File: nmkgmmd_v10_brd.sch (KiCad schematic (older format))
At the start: 3 parts

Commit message: 石を303CC(48pin)に変更，少しだけピンを引き出した
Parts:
- removed C? (x2): C, symbol C
- removed U?: STM32F303RETx, LQFP64, symbol STM32F303RETx
- added L?: L, symbol L
- added U?: STM32F313CCTx, LQFP48, symbol STM32F313CCTx
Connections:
- net labels added: ADC1_IN1, ADC1_IN2, ADC2_IN1, ADC3_IN1, ADC4_IN3, GD_FAULT1, GD_FAULT2, GD_RESET1, GD_RESET2, LED0, LED1, LED2, SWCLK, SWDIO, TIM15_CH2, TIM1_CH1, TIM1_CH1N, TIM1_CH2, TIM1_CH2N, TIM2_CH1, TIM2_CH2, TIM3_CH1, TIM3_CH2, TIM4_CH2, TIM8_CH1, TIM8_CH1N, TIM8_CH2, TIM8_CH2N, USART3RX, USART3TX
- wire segments 29 -> 23
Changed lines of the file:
@@
 LIBS:valves
 LIBS:stm32
+LIBS:nmkgmmd_v10_brd-cache
 EELAYER 25 0
 EELAYER END
@@
 Comment4 ""
 $EndDescr
-$Comp
-L STM32F303RETx U?
-U 1 1 58989F63
-P 8250 5300
-F 0 "U?" H 3150 7225 50  0000 L BNN
-F 1 "STM32F303RETx" H 13350 7225 50  0000 R BNN
-F 2 "LQFP64" H 13350 7175 50  0000 R TNN
-F 3 "" H 8250 5300 50  0000 C CNN
-	1    8250 5300
-	1    0    0    -1
-$EndComp
 $Comp
 L GND #PWR?
@@
 	1    0    0    -1
 $EndComp
-$Comp
-L C C?
-U 1 1 5898A2BF
-P 1700 4800
-F 0 "C?" H 1725 4900 50  0000 L CNN
-F 1 "C" H 1725 4700 50  0000 L CNN
-F 2 "" H 1738 4650 50  0001 C CNN
-F 3 "" H 1700 4800 50  0001 C CNN
-	1    1700 4800
-	0    1    1    0
-$EndComp
-$Comp
-L C C?
-U 1 1 5898A3A8
-P 1700 5100
-F 0 "C?" H 1725 5200 50  0000 L CNN
-F 1 "C" H 1725 5000 50  0000 L CNN
-F 2 "" H 1738 4950 50  0001 C CNN
-F 3 "" H 1700 5100 50  0001 C CNN
-	1    1700 5100
-	0    1    1    0
-$EndComp
-$Comp
-L GND #PWR?
-U 1 1 5898A3C8
-P 1450 4950
-F 0 "#PWR?" H 1450 4700 50  0001 C CNN
-F 1 "GND" H 1450 4800 50  0000 C CNN
-F 2 "" H 1450 4950 50  0001 C CNN
-F 3 "" H 1450 4950 50  0001 C CNN
-	1    1450 4950
-	0    1    1    0
-$EndComp
 Wire Wire Line
 	8050 7300 8050 7350
 Wire Wire Line
-	8050 7350 8150 7350
+	8050 7350 8350 7350
 Wire Wire Line
-	8150 7350 8200 7350
+	8350 7350 8350 7100
 Wire Wire Line
-	8200 7350 8250 7350
-Wire Wire Line
-	8250 7350 8350 7350
-Wire Wire Line
-	8350 7350 8350 7300
-Wire Wire Line
-	8150 7300 8150 7350
+	8150 7100 8150 7350
 Connection ~ 8150 7350
 Wire Wire Line
-	8250 7300 8250 7350
+	8250 7100 8250 7350
 Connection ~ 8250 7350
 Wire Wire Line
@@
 Connection ~ 8200 7350
 Wire Wire Line
-	8050 3300 8050 3250
-Wire Wire Line
-	8050 3250 8150 3250
-Wire Wire Line
-	8150 3250 8200 3250
-Wire Wire Line
-	8200 3250 8250 3250
-Wire Wire Line
-	8250 3250 8350 3250
+	8100 3250 8350 3250
 Wire Wire Line
 	8350 3250 8350 3300
@@
 Connection ~ 8200 3250
 Wire Wire Line
-	1550 4800 1500 4800
-Wire Wire Line
-	1500 4800 1500 4950
-Wire Wire Line
-	1500 4950 1500 5100
-Wire Wire Line
-	1500 5100 1550 5100
-Wire Wire Line
-	1450 4950 1500 4950
-Connection ~ 1500 4950
-Wire Wire Line
 	3050 5000 2350 5000
 Wire Wire Line
@@
 Wire Wire Line
 	2350 4800 2000 4800
+$Comp
+L STM32F313CCTx U?
+U 1 1 58ADBEE3
+P 8250 5200
+F 0 "U?" H 1750 7025 50  0000 L BNN
+F 1 "STM32F313CCTx" H 14750 7025 50  0000 R BNN
+F 2 "LQFP48" H 14750 6975 50  0001 R TNN
+F 3 "" H 8250 5200 50  0001 C CNN
+	1    8250 5200
+	1    0    0    -1
+$EndComp
+$Comp
+L L L?
+U 1 1 58ADC12E
+P 7850 3050
+F 0 "L?" V 7800 3050 50  0000 C CNN
+F 1 "L" V 7925 3050 50  0000 C CNN
+F 2 "" H 7850 3050 50  0001 C CNN
+F 3 "" H 7850 3050 50  0001 C CNN
+	1    7850 3050
+	0    -1   -1   0
+$EndComp
+Wire Wire Line
+	8100 3250 8100 3050
+Wire Wire Line
+	8100 3050 8000 3050
+Wire Wire Line
+	7700 3050 7650 3050
+Wire Wire Line
+	7650 3050 7650 3250
+Wire Wire Line
+	7650 3250 8050 3250
+Wire Wire Line
+	8050 3250 8050 3300
+Text HLabel 14850 5100 2    60   Input ~ 0
+ADC1_IN1
+Text HLabel 14850 5200 2    60   Input ~ 0
+ADC1_IN2
+Text HLabel 14850 5500 2    60   Input ~ 0
+ADC2_IN1
+Text HLabel 14850 5800 2    60   Output ~ 0
+TIM8_CH1N
+Text HLabel 14850 5900 2    60   Output ~ 0
+TIM1_CH1
+Text HLabel 14850 6000 2    60   Output ~ 0
+TIM1_CH2
+Text HLabel 14850 6100 2    60   Output ~ 0
+GD_RESET1
+Text HLabel 14850 6200 2    60   Output ~ 0
+GD_RESET2
+Text HLabel 14850 6300 2    60   Output ~ 0
+TIM1_CH2N
+Text GLabel 14850 6400 2    60   Input ~ 0
+SWDIO
+Text GLabel 14850 6500 2    60   Input ~ 0
+SWCLK
+Text HLabel 14850 6600 2    60   Output ~ 0
+TIM2_CH1
+Text HLabel 1650 6600 0    60   Input ~ 0
+TIM15_CH2
+Text HLabel 1650 6500 0    60   Input ~ 0
+GD_FAULT1
+Text HLabel 1650 6400 0    60   Input ~ 0
+GD_FAULT2
+Text HLabel 1650 6300 0    60   Input ~ 0
+ADC4_IN3
+Text HLabel 1650 6200 0    60   Input ~ 0
+USART3RX
+Text HLabel 1650 6100 0    60   Output ~ 0
+USART3TX
+Text HLabel 1650 6000 0    60   Output ~ 0
+LED0
+Text HLabel 1650 5900 0    60   Output ~ 0
+TIM8_CH2
+Text HLabel 1650 5800 0    60   Output ~ 0
+TIM4_CH2
+Text HLabel 1650 5700 0    60   Output ~ 0
+TIM8_CH1
+Text HLabel 1650 5600 0    60   Input ~ 0
+TIM3_CH2
+Text HLabel 1650 5500 0    60   Input ~ 0
+TIM3_CH1
+Text HLabel 1650 5400 0    60   Input ~ 0
+TIM2_CH2
+Text HLabel 1650 5300 0    60   Input ~ 0
+ADC3_IN1
+Text HLabel 1650 5200 0    60   Output ~ 0
+TIM8_CH2N
+Text HLabel 1650 4800 0    60   Output ~ 0
+TIM1_CH1N
+Text HLabel 1650 4900 0    60   Output ~ 0
+LED1
+Text HLabel 1650 5000 0    60   Output ~ 0
+LED2
 $EndSCHEMATC

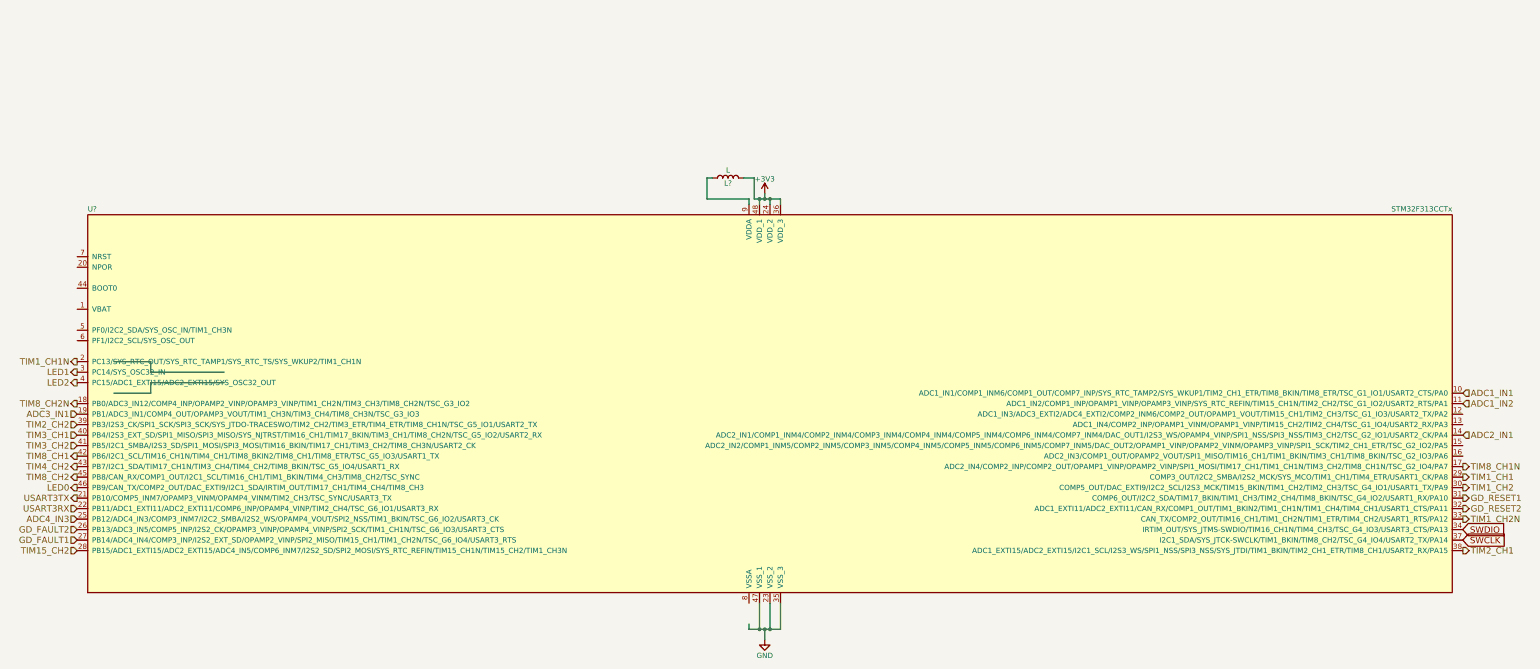
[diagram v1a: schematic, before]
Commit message: 制御回路完成，アノテーション
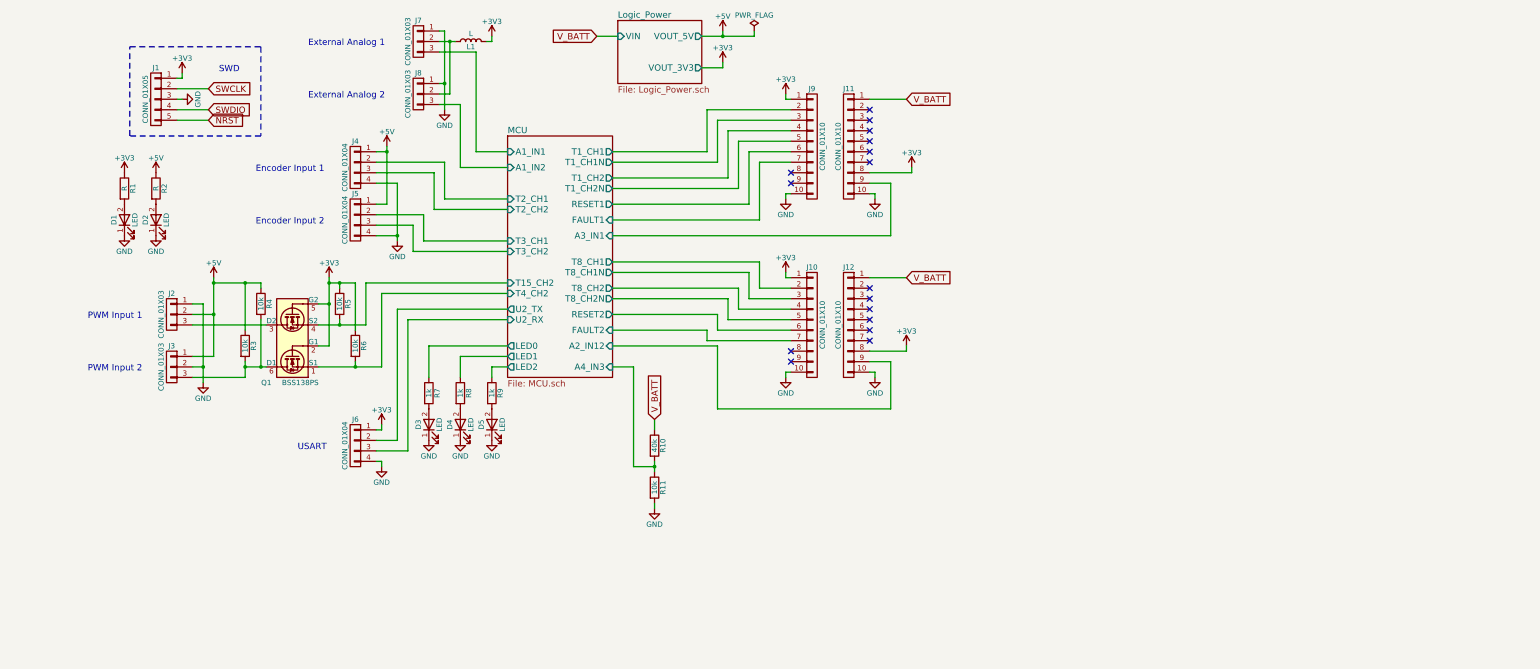
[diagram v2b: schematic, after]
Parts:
- removed L?: L, symbol L
- removed U?: STM32F313CCTx, LQFP48, symbol STM32F313CCTx
- added D1, D2, D3, D4, D5: LED, LEDs:LED_0603, symbol LED
- added J1: CONN_01X05, Connectors_JST:JST_ZH_S05B-ZR_05x1.50mm_Angled, symbol CONN_01X05
- added J10, J11, J12, J9: CONN_01X10, Pin_Headers:Pin_Header_Straight_1x10_Pitch2.00mm, symbol CONN_01X10
- added J2, J3, J7, J8: CONN_01X03, Connectors_JST:JST_ZH_S03B-ZR_03x1.50mm_Angled, symbol CONN_01X03
- added J4, J5, J6: CONN_01X04, Connectors_JST:JST_ZH_S04B-ZR_04x1.50mm_Angled, symbol CONN_01X04
- added L1: L, Inductors_NEOSID:Neosid_Inductor_SM0603CG, symbol L
- added Q1: BSS138PS, TO_SOT_Packages_SMD:SOT-363_SC-70-6, symbol BSS138PS
- added R1, R2: R, Resistors_SMD:R_0603, symbol R
- added R10: 40k, Resistors_SMD:R_0603, symbol R
- added R11, R3, R4, R5, R6: 10k, Resistors_SMD:R_0603, symbol R
- added R7, R8, R9: 1k, Resistors_SMD:R_0603, symbol R
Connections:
- net labels added: +5V, NRST, V_BATT
- net labels removed: ADC1_IN1, ADC1_IN2, ADC2_IN1, ADC3_IN1, ADC4_IN3, GD_FAULT1, GD_FAULT2, GD_RESET1, GD_RESET2, LED0, LED1, LED2, TIM15_CH2, TIM1_CH1, TIM1_CH1N, TIM1_CH2, TIM1_CH2N, TIM2_CH1, TIM2_CH2, TIM3_CH1, TIM3_CH2, TIM4_CH2, TIM8_CH1, TIM8_CH1N, TIM8_CH2, TIM8_CH2N, USART3RX, USART3TX
- wire segments 23 -> 156
- no-connect marks 0 -> 16
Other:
- note added: "Encoder Input 1"
- note added: "Encoder Input 2"
- note added: "External Analog 1"
- note added: "External Analog 2"
- note added: "PWM Input 1"
- note added: "PWM Input 2"
- note added: "SWD"
- note added: "USART"

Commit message: 回路図作ってみた
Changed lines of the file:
@@
 $Descr A4 11693 8268
 encoding utf-8
-Sheet 1 3
+Sheet 1 5
 Title ""
 Date ""
@@
 Wire Wire Line
 	7650 4500 6750 4500
+$Sheet
+S 9500 5550 1200 800
+U 58CBAEB3
+F0 "Driver1" 60
+F1 "Driver.sch" 60
+$EndSheet
+$Sheet
+S 7950 5550 1400 800
+U 58CBB47A
+F0 "Driver2" 60
+F1 "Driver.sch" 60
+$EndSheet
 $EndSCHEMATC

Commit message: アノテーション前のセーブ
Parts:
- removed J11, J12: CONN_01X10, Pin_Headers:Pin_Header_Straight_1x10_Pitch2.00mm, symbol CONN_01X10
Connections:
- net +3V3: now also J10.5 (P5), J9.5 (P5); no longer J10.1 (P1), J9.1 (P1)
- net GND: now also J10.3 (P3), J9.3 (P3); no longer J10.10 (P10), J9.10 (P10)
- net MCU/A2_IN12: now also J10.1 (P1)
- net MCU/A3_IN1: now also J9.1 (P1)
- net MCU/FAULT1: now also J9.6 (P6); no longer J9.7 (P7)
- net MCU/FAULT2: now also J10.6 (P6); no longer J10.7 (P7)
- net MCU/RESET1: now also J9.4 (P4); no longer J9.6 (P6)
- net MCU/RESET2: now also J10.4 (P4); no longer J10.6 (P6)
- net MCU/T1_CH1: now also J9.7 (P7); no longer J9.2 (P2)
- net MCU/T1_CH1N: now also J9.8 (P8); no longer J9.3 (P3)
- net MCU/T1_CH2: now also J9.9 (P9); no longer J9.4 (P4)
- net MCU/T1_CH2N: now also J9.10 (P10); no longer J9.5 (P5)
- net MCU/T8_CH1: now also J10.7 (P7); no longer J10.2 (P2)
- net MCU/T8_CH1N: now also J10.8 (P8); no longer J10.3 (P3)
- net MCU/T8_CH2: now also J10.9 (P9); no longer J10.4 (P4)
- net MCU/T8_CH2N: now also J10.10 (P10); no longer J10.5 (P5)
- net V_BATT: now also J10.2 (P2), J9.2 (P2)
- no-connect marks 16 -> 0
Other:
- moved on the sheet: J9

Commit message: セーブ
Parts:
- J10, J9: footprint Pin_Headers:Pin_Header_Straight_1x10_Pitch2.00mm -> Pin_Headers:Pin_Header_Straight_1x10_Pitch2.00mm_SMD_Pin1Right
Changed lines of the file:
@@
 F 0 "J9" H 8700 3250 50  0000 C CNN
 F 1 "CONN_01X10" V 8800 2700 50  0000 C CNN
-F 2 "Pin_Headers:Pin_Header_Straight_1x10_Pitch2.00mm" H 8700 2700 50  0001 C CNN
+F 2 "Pin_Headers:Pin_Header_Straight_1x10_Pitch2.00mm_SMD_Pin1Right" H 8700 2700 50  0001 C CNN
 F 3 "" H 8700 2700 50  0001 C CNN
 	1    8700 2700
@@
 F 0 "J10" H 8650 5000 50  0000 C CNN
 F 1 "CONN_01X10" V 8750 4450 50  0000 C CNN
-F 2 "Pin_Headers:Pin_Header_Straight_1x10_Pitch2.00mm" H 8650 4450 50  0001 C CNN
+F 2 "Pin_Headers:Pin_Header_Straight_1x10_Pitch2.00mm_SMD_Pin1Right" H 8650 4450 50  0001 C CNN
 F 3 "" H 8650 4450 50  0001 C CNN
 	1    8650 4450
@@
 V_BATT
 $Comp
-L GND #PWR026
+L GND #PWR023
 U 1 1 58C4425D
 P 8450 4200
-F 0 "#PWR026" H 8450 3950 50  0001 C CNN
+F 0 "#PWR023" H 8450 3950 50  0001 C CNN
 F 1 "GND" H 8450 4050 50  0000 C CNN
 F 2 "" H 8450 4200 50  0001 C CNN
@@
 $EndComp
 $Comp
-L GND #PWR029
+L GND #PWR024
 U 1 1 58C68B7D
 P 7150 6200
-F 0 "#PWR029" H 7150 5950 50  0001 C CNN
+F 0 "#PWR024" H 7150 5950 50  0001 C CNN
 F 1 "GND" H 7150 6050 50  0000 C CNN
 F 2 "" H 7150 6200 50  0001 C CNN
@@
 	7800 2000 7600 2000
 $Comp
-L PWR_FLAG #FLG030
+L PWR_FLAG #FLG025
 U 1 1 58CAB0FE
 P 8100 1650
-F 0 "#FLG030" H 8100 1725 50  0001 C CNN
+F 0 "#FLG025" H 8100 1725 50  0001 C CNN
 F 1 "PWR_FLAG" H 8100 1800 50  0000 C CNN
 F 2 "" H 8100 1650 50  0001 C CNN
@@
 $EndSheet
 $Comp
-L +3V3 #PWR025
+L +3V3 #PWR026
 U 1 1 58C42440
 P 8450 4400
-F 0 "#PWR025" H 8450 4250 50  0001 C CNN
+F 0 "#PWR026" H 8450 4250 50  0001 C CNN
 F 1 "+3V3" H 8450 4540 50  0000 C CNN
 F 2 "" H 8450 4400 50  0001 C CNN

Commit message: 進捗，セーブ
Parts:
- J1: footprint Connectors_JST:JST_ZH_S05B-ZR_05x1.50mm_Angled -> Connectors_JST:JST_SH_BM05B-SRSS-TB_05x1.00mm_Straight
- J6: footprint Connectors_JST:JST_ZH_S04B-ZR_04x1.50mm_Angled -> Connectors_JST:JST_ZH_B04B-ZR_04x1.50mm_Straight
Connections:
- net at J2.3 (P3), Q1.3 (D2): now also R4.2
- net at J3.3 (P3), Q1.6 (D1), R3.2: no longer R4.2
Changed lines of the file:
@@
 F 0 "J6" H 4300 5850 50  0000 C CNN
 F 1 "CONN_01X04" V 4400 5600 50  0000 C CNN
-F 2 "Connectors_JST:JST_ZH_S04B-ZR_04x1.50mm_Angled" H 4300 5600 50  0001 C CNN
+F 2 "Connectors_JST:JST_ZH_B04B-ZR_04x1.50mm_Straight" H 4300 5600 50  0001 C CNN
 F 3 "" H 4300 5600 50  0001 C CNN
 	1    4300 5600
@@
 F 0 "J1" H 2400 2600 50  0000 C CNN
 F 1 "CONN_01X05" V 2500 2300 50  0000 C CNN
-F 2 "Connectors_JST:JST_ZH_S05B-ZR_05x1.50mm_Angled" H 2400 2300 50  0001 C CNN
+F 2 "Connectors_JST:JST_SH_BM05B-SRSS-TB_05x1.00mm_Straight" H 2400 2300 50  0001 C CNN
 F 3 "" H 2400 2300 50  0001 C CNN
 	1    2400 2300
@@
 Connection ~ 3250 4850
 Wire Wire Line
-	3400 4400 3400 4850
-Connection ~ 3400 4850
-Wire Wire Line
 	3250 4050 3250 4500
 Wire Wire Line
@@
 Wire Wire Line
 	7550 3850 6750 3850
+Wire Wire Line
+	3400 4400 3400 4450
+Connection ~ 3400 4450
 $EndSCHEMATC

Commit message: 進捗
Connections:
- net +5V: now also J3.2 (P2); no longer J3.1 (P1)
- net GND: now also J3.1 (P1); no longer J3.2 (P2)
- net MCU/T3_CH1: now also J5.3 (P3); no longer J5.2 (P2)
- net MCU/T3_CH2: now also J5.2 (P2); no longer J5.3 (P3)
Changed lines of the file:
@@
 	4600 2750 4600 3300
-Wire Wire Line
-	4500 3400 4950 3400
-Wire Wire Line
-	4500 3500 4850 3500
 Wire Wire Line
 	4600 3300 4500 3300
@@
 	5750 4150 4550 4150
 Wire Wire Line
-	4550 4150 4550 4850
+	4550 4850 4550 4150
 Wire Wire Line
 	4400 4050 5750 4050
@@
 	2850 4250 2850 5000
 Wire Wire Line
-	2850 4850 2750 4850
-Wire Wire Line
-	2950 4750 2750 4750
-Wire Wire Line
-	2950 4000 2950 4750
+	2950 4000 2950 4850
 Wire Wire Line
 	2950 4350 2750 4350
-Connection ~ 2850 4850
 Connection ~ 2950 4350
 Wire Wire Line
-	5750 3750 4850 3750
-Wire Wire Line
-	4850 3750 4850 3500
-Wire Wire Line
-	4950 3400 4950 3650
+	4850 3750 5750 3750
+Wire Wire Line
+	4850 3400 4850 3750
+Wire Wire Line
+	4950 3500 4950 3650
 Wire Wire Line
 	4950 3650 5750 3650
@@
 Connection ~ 3250 4050
 Wire Wire Line
-	4550 4850 3950 4850
+	3950 4850 4550 4850
 Wire Wire Line
 	4300 4800 4300 4850
@@
 	3400 4400 3400 4450
 Connection ~ 3400 4450
+Wire Wire Line
+	2950 4850 2750 4850
+Wire Wire Line
+	2750 4750 2850 4750
+Connection ~ 2850 4750
+Wire Wire Line
+	4850 3400 4500 3400
+Wire Wire Line
+	4950 3500 4500 3500
 $EndSCHEMATC

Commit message: 進捗
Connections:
- net MCU/T2_CH1: now also J4.3 (P3); no longer J4.2 (P2)
- net MCU/T2_CH2: now also J4.2 (P2); no longer J4.3 (P3)
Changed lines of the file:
@@
 	4950 3650 5750 3650
 Wire Wire Line
-	5050 3000 5050 3350
-Wire Wire Line
-	5050 3350 5750 3350
+	5150 3350 5750 3350
 Wire Wire Line
 	4500 2900 5150 2900
 Wire Wire Line
-	5150 2900 5150 3250
-Wire Wire Line
-	5150 3250 5750 3250
+	5050 3250 5750 3250
 Wire Wire Line
 	5300 2950 5750 2950
@@
 Wire Wire Line
 	4950 3500 4500 3500
+Wire Wire Line
+	5050 3000 5050 3250
+Wire Wire Line
+	5150 2900 5150 3350
 $EndSCHEMATC
